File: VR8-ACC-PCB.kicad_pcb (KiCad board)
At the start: 2 copper layers, 140 x 60 mm, 66 parts, among them IC1 LM393P, IC2 VO14642AT, IC3 VO14642AT, IC4 KT12-1A-40L-THT, IC5 NE555P, J1 43650-0516, J2 43650-0516, J3 43650-0216, J4 43650-0416, J5 43045-1013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

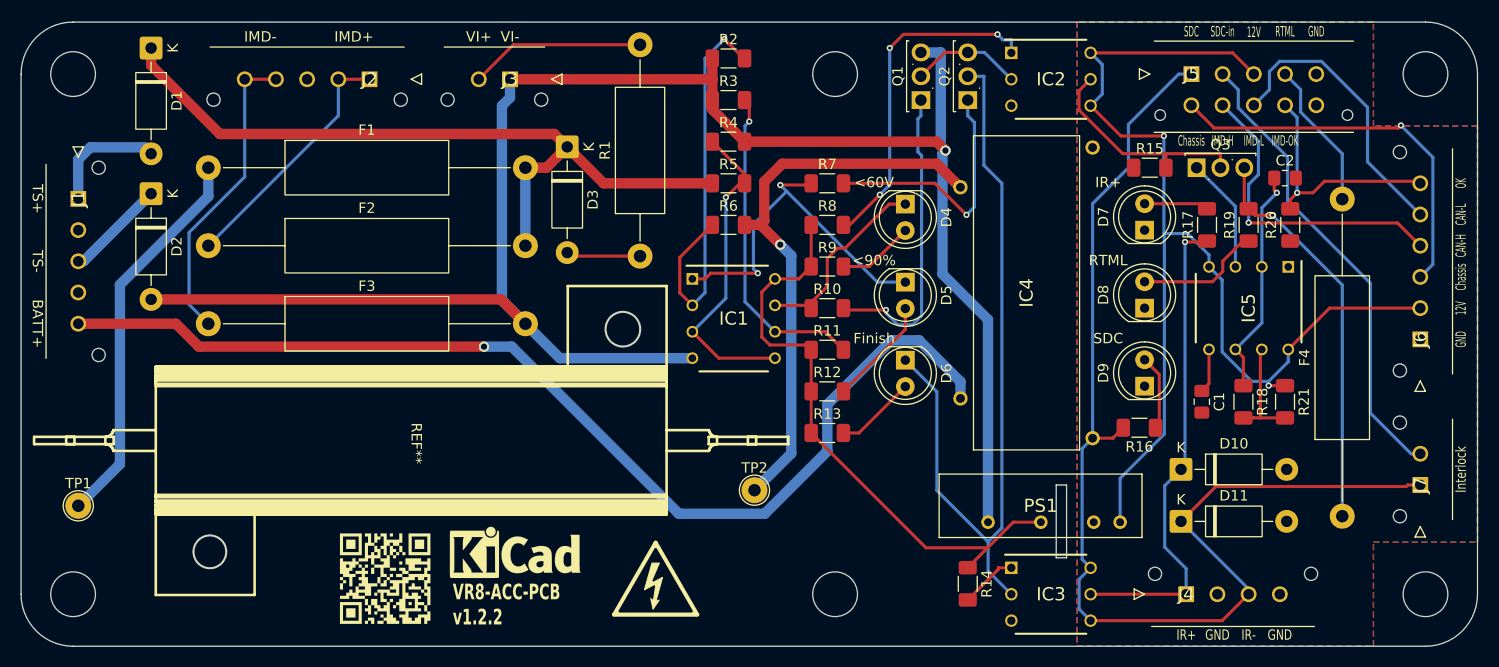
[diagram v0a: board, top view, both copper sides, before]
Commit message: J5 reorientation
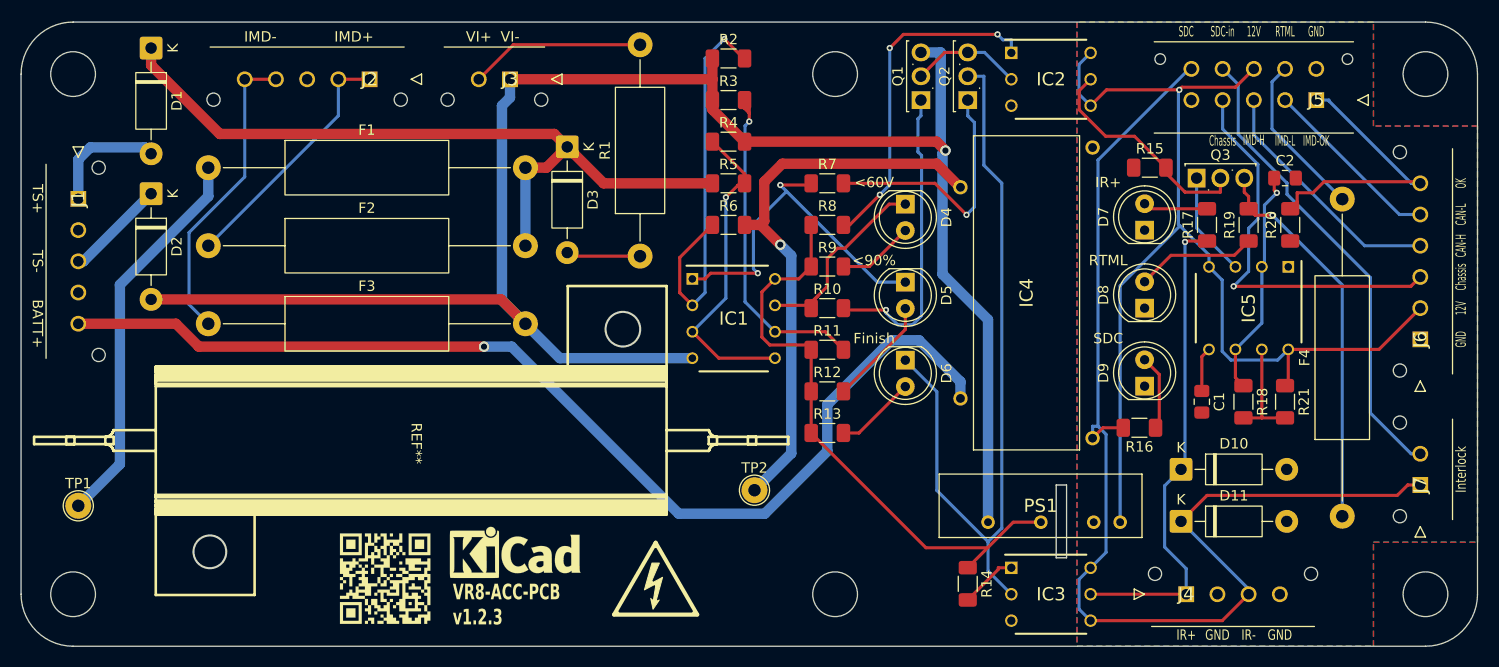
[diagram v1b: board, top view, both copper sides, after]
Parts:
- moved J5 12.3 mm to (160.0, 42.5), turned to 0 degrees
- moved Q3 1.00 mm to (148.5, 50.0)
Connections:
- J5 pad 1: SDC_final -> IMD_Status
- J5 pad 10: unconnected-(J5-Pad10) -> SDC_final
- J5 pad 2: SDC_after_MSD -> IMD_CAN_L
- J5 pad 3: GLV_12V -> IMD_CAN_H
- J5 pad 4: RTML -> Chassis_Ground
- J5 pad 5: GND -> unconnected-(J5-Pad5)
- J5 pad 6: Chassis_Ground -> GND
- J5 pad 7: IMD_CAN_H -> RTML
- J5 pad 8: IMD_CAN_L -> GLV_12V
- J5 pad 9: IMD_Status -> SDC_after_MSD
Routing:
- net IMD_CAN_L: track 27.9 -> 17.6 mm
- net IMD_CAN_H: track 30.5 -> 23.8 mm, vias 1 -> 0
- net GLV_12V: track 110.5 -> 105.6 mm, vias 2 -> 1
- net IMD_Status: track 22.8 -> 27.3 mm, vias 1 -> 0
- net RTML: track 14.3 -> 15.8 mm
- net Net-(IC1-2IN-): track 30.5 -> 31.9 mm
- net SDC_final: track 112.1 -> 113.4 mm
- net Chassis_Ground: track 37.5 -> 38.6 mm
- net Net-(IC5-OUT): track 11.1 -> 10.1 mm
- net OK_60V: track 18.1 -> 19.0 mm
- net SDC_after_MSD: track 44.9 -> 45.4 mm
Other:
- board text added: "VR8-ACC-PCB v1.2.3"
- board text removed: "VR8-ACC-PCB v1.2.2"

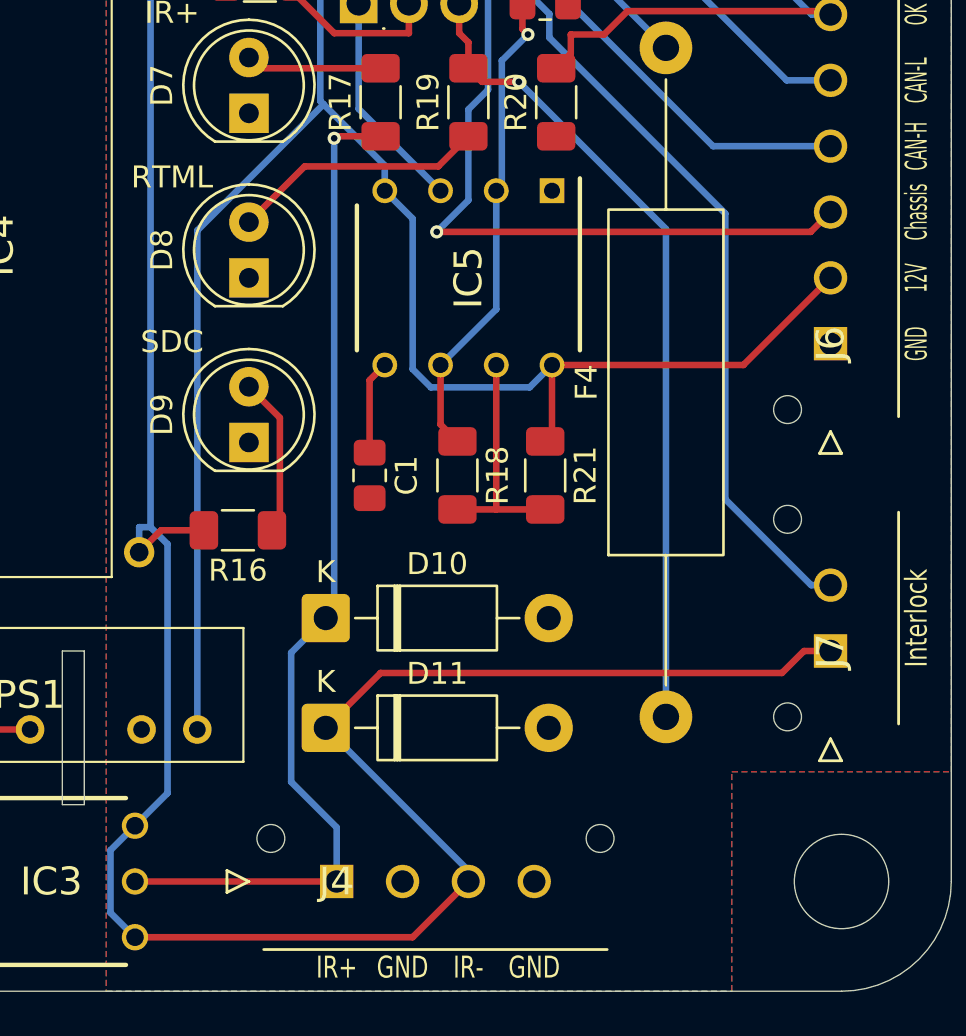
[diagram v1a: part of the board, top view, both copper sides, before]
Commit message: J4 reorientation
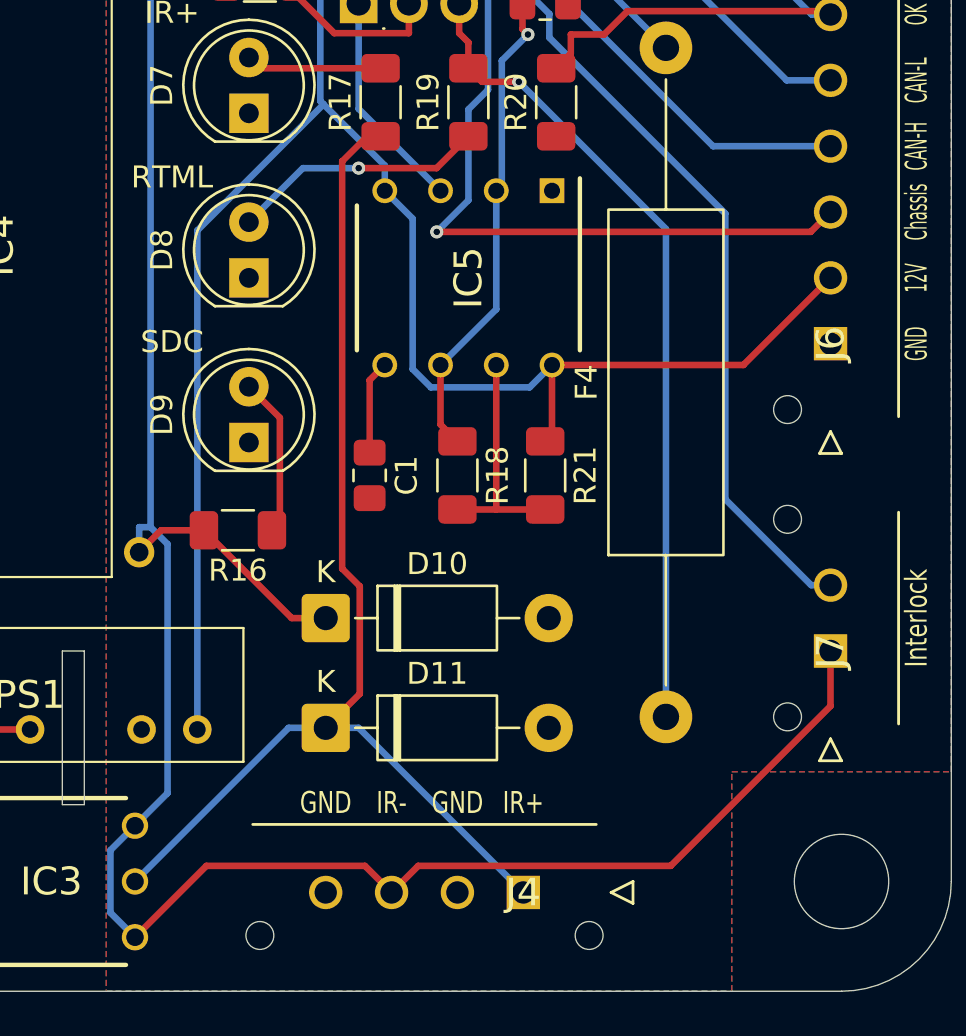
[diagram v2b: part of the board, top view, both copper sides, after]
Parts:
- moved J4 8.51 mm to (156.0, 90.5), turned to 0 degrees
- moved D10 5.00 mm to (147.0, 78.0)
- moved D11 5.00 mm to (147.0, 83.0)
- renumbered D11 to D10, D10 to D11
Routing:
- net IR+_ctrl: track 46.3 -> 52.1 mm, vias 1 -> 0
- net SDC_final: track 113.4 -> 110.3 mm
- net Net-(D8-A): vias 0 -> 1

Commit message: update version
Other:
- board text added: "VR8-ACC-PCB v1.2.4"
- board text removed: "VR8-ACC-PCB v1.2.3"
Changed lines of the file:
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@@
 		)
 	)
-	(gr_text "VR8-ACC-PCB\nv1.2.3"
+	(gr_text "VR8-ACC-PCB\nv1.2.4"
 		(at 77 91 0)
 		(layer "F.SilkS")

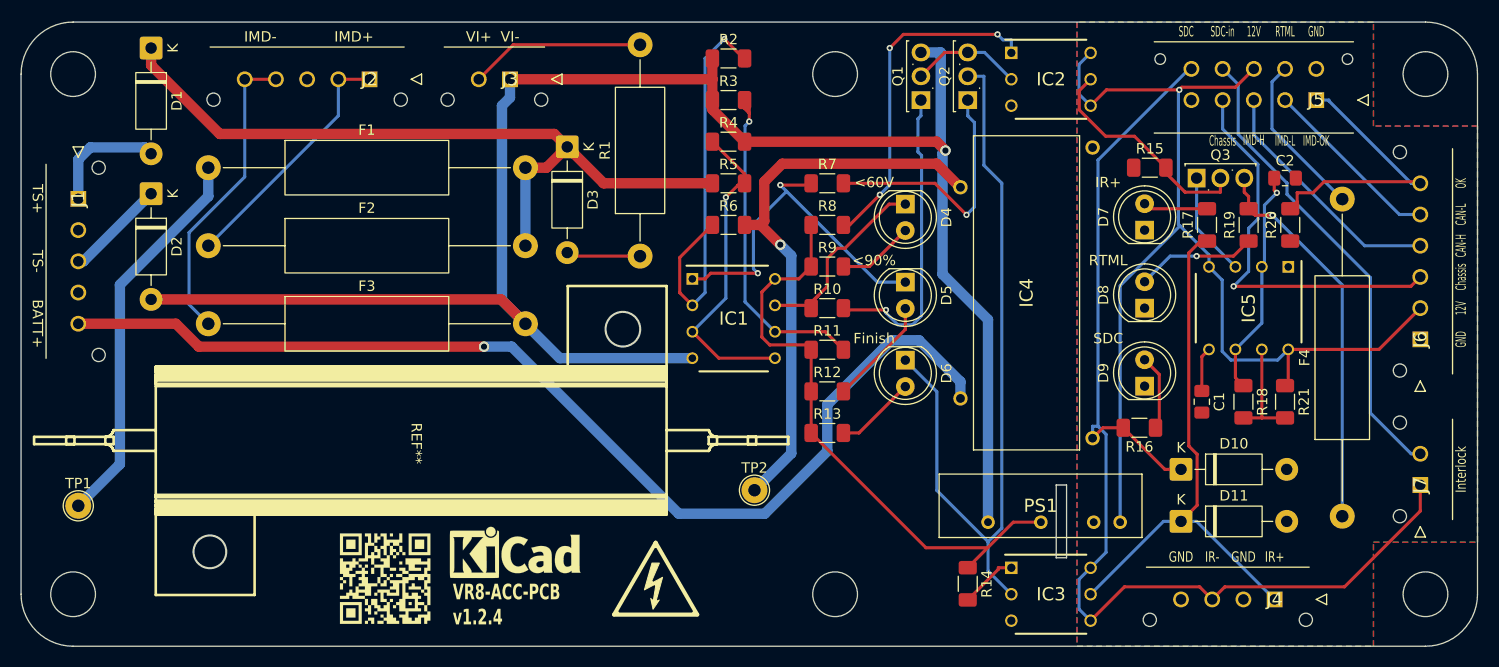
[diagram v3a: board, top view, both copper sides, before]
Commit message: add ne555 output resister
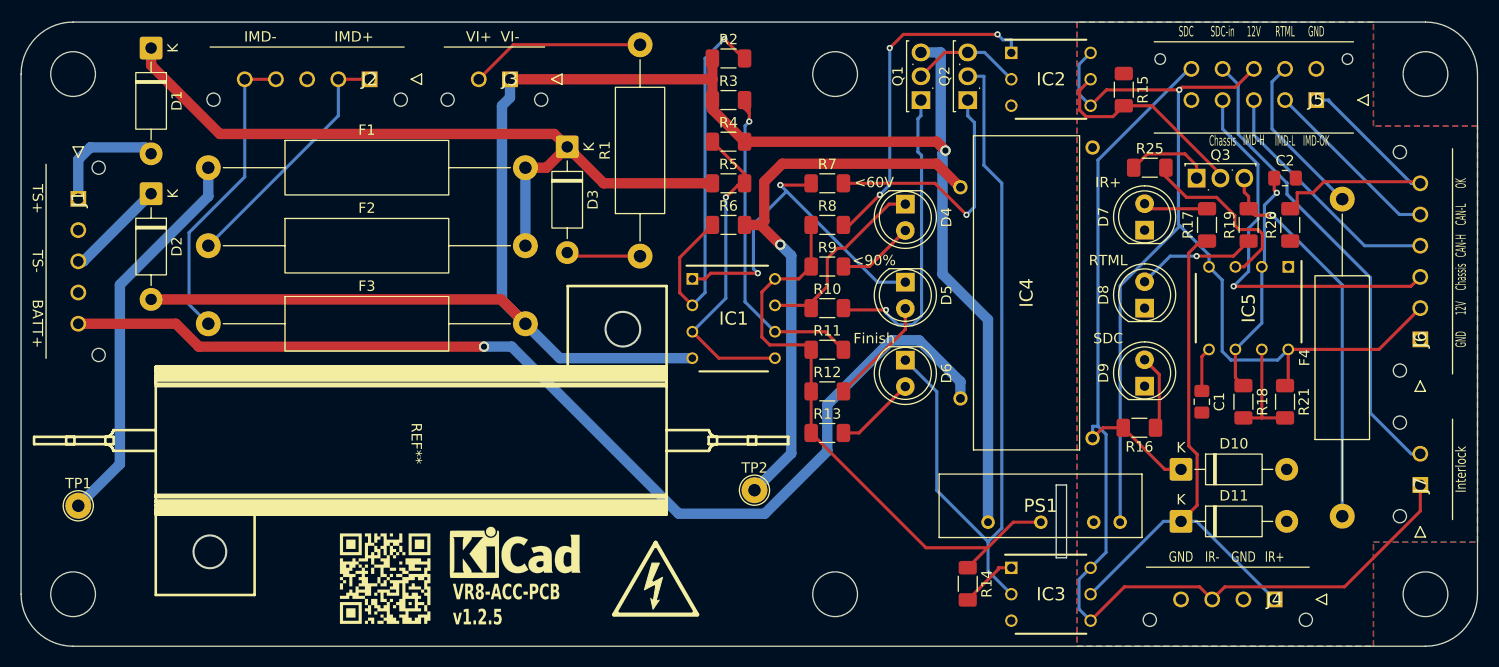
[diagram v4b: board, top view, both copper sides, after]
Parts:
- added R25: 10k, Resistor_SMD:R_1206_3216Metric_Pad1.30x1.75mm_HandSolder, F.Cu at (144.0, 49.0)
- moved R15 7.91 mm to (141.5, 41.5), turned to -90 degrees
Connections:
- Q3 pad 1: Net-(IC5-OUT) -> Net-(Q3-G)
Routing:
- net Net-(Q3-G): track 0.00 -> 8.27 mm
- net Net-(IC5-OUT): track 10.1 -> 17.7 mm
- net RTML_enable: track 21.4 -> 20.7 mm
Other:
- board text added: "GLV"
- board text added: "VR8-ACC-PCB v1.2.5"
- board text removed: "LV"
- board text removed: "VR8-ACC-PCB v1.2.4"

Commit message: fix wrong DCDC & precharge relay pin connection
swap out +/out - of the DCDC
swap coil/contact of the relay
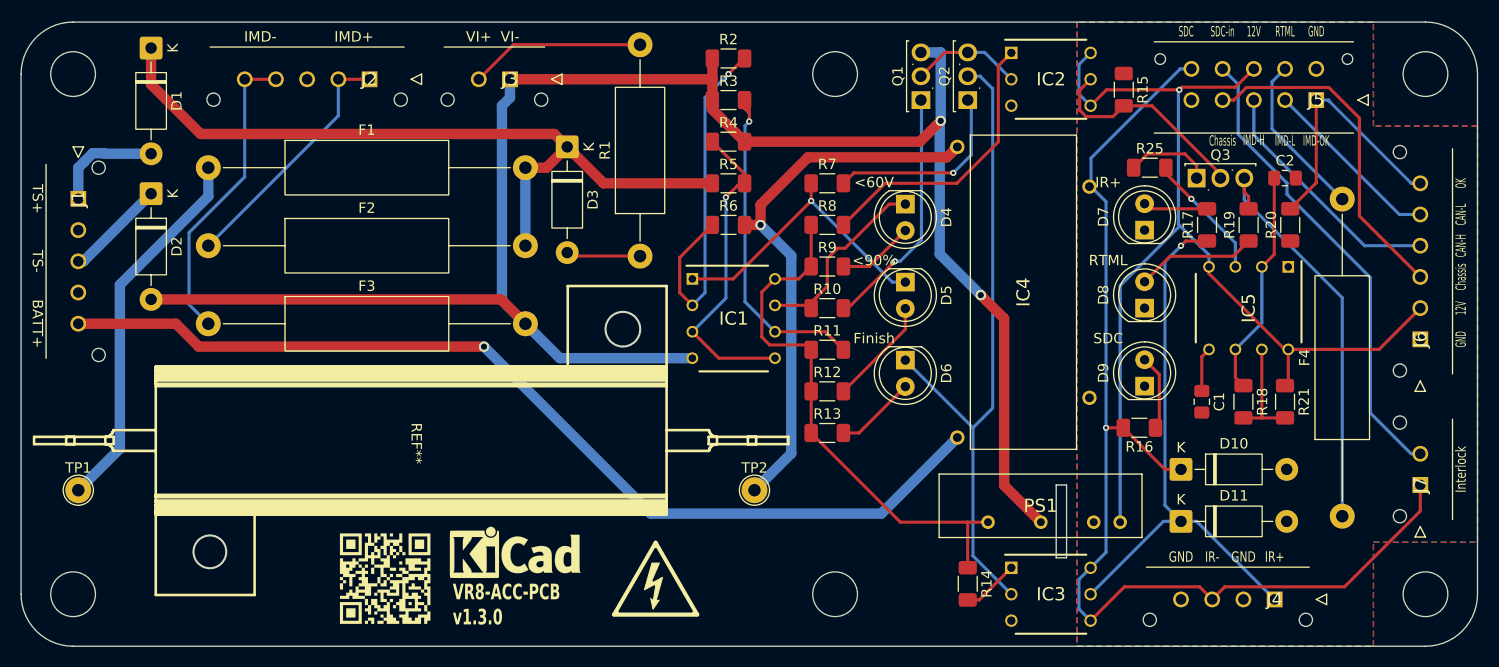
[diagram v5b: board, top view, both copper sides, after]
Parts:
- moved IC4 30.9 mm to (125.5, 47.0), turned to -90 degrees
- moved TP1 1.50 mm to (41.0, 80.0)
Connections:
- IC4 pad 1: SDC_final -> HV+
- IC4 pad 2: GND -> BATT+
- IC4 pad 3: HV+ -> GND
- IC4 pad 4: BATT+ -> SDC_final
- PS1 pad 4: HV_12V -> TS-
- PS1 pad 6: TS- -> HV_12V
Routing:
- net Net-(D6-K): track 74.3 -> 63.0 mm
- net BATT+: track 105.2 -> 95.1 mm
- net Net-(Q2-G): track 24.7 -> 18.3 mm
- net OK_90%: track 34.6 -> 28.3 mm, vias 2 -> 1
- net Chassis_Ground: track 38.6 -> 32.6 mm, vias 1 -> 0
- net Net-(Q1-G): track 29.4 -> 23.4 mm
- net Net-(IC5-OUT): track 17.7 -> 11.7 mm, vias 0 -> 1
- net Net-(IC2-A): track 32.9 -> 27.3 mm, vias 3 -> 0
- net HV_12V: track 57.1 -> 51.6 mm
- net GLV_12V: track 105.6 -> 100.8 mm
- net Net-(IC1-1IN-): track 39.0 -> 35.3 mm
- net IMD_Status: track 27.3 -> 24.8 mm
- net Net-(Q3-S): track 37.4 -> 39.5 mm, vias 1 -> 0
- net SDC_final: track 110.3 -> 108.2 mm, vias 0 -> 1
- net IR+_ctrl: track 52.1 -> 54.2 mm, vias 0 -> 1
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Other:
- board text added: "VR8-ACC-PCB v1.3.0"
- board text removed: "VR8-ACC-PCB v1.2.5"

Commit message: find and fix test errors, some improvement
1. remove onboard fuse (now is inline)
2. change RTML nmos to pmos (to make nmos on, RTML only have V_G-V_th=10V, which is not enough to drive RTML)
3. new voltage divider config (resistors tolerance is matter, <1% is better)
4. add IR+_ctrl signal output to J5
5. J7 is now used for powering Arduino rather than bridging interlock signal (SDC_after_MSD is removed from J5 as well)
6. explain the working principle on sch
7. move to kicad 10
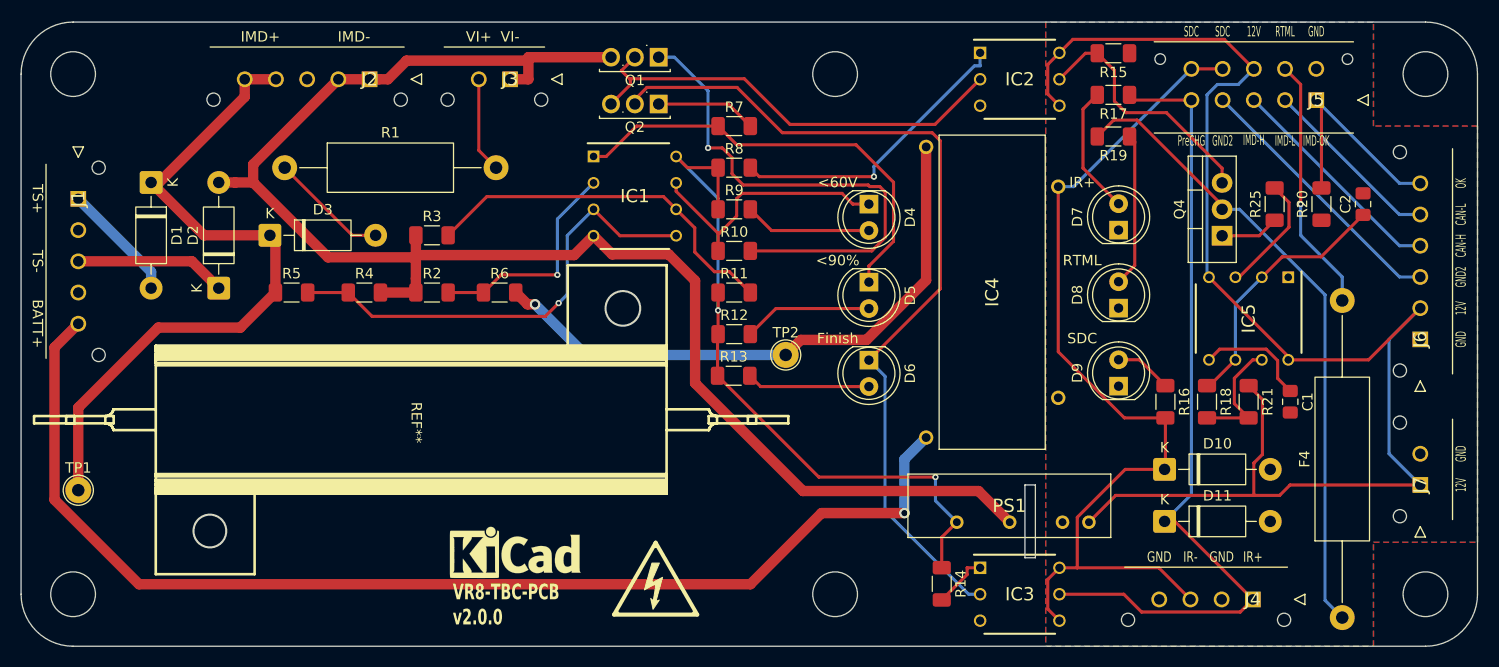
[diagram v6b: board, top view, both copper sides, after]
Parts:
- removed F1, F2, F3: Fuse, Resistor_THT:R_Axial_DIN0516_L15.5mm_D5.0mm_P30.48mm_Horizontal
- removed Q3: Q_NMOS_Depletion_GDS, Package_TO_SOT_THT:TO-251-3_Vertical
- removed QR*****: github, custom:github
- added Q4: Q_PMOS_GDS, Package_TO_SOT_THT:TO-220-3_Vertical, F.Cu at (150.9, 55.5)
- R1: value 360k -> 200k
- moved R5 43.3 mm to (61.5, 61.0)
- moved R4 37.9 mm to (68.5, 61.0)
- moved R2 36.3 mm to (75.0, 61.0)
- moved R1 35.2 mm to (60.8, 49.0), turned to 0 degrees
- moved R3 31.3 mm to (75.0, 55.5)
- moved D3 29.8 mm to (59.4, 55.5), turned to 0 degrees
- moved Q2 29.7 mm to (96.8, 42.9), turned to 180 degrees
- moved Q1 25.5 mm to (96.8, 38.4), turned to 180 degrees
- moved R6 22.9 mm to (81.5, 61.0)
- moved R19 15.5 mm to (140.5, 46.0), turned to 180 degrees
- moved R17 15.4 mm to (140.5, 42.0), turned to 180 degrees
- moved IC1 15.1 mm to (94.5, 51.7)
- moved TP2 13.3 mm to (109.0, 67.0)
- moved D1 12.9 mm to (48.0, 50.4)
- moved R25 12.5 mm to (156.0, 52.5), turned to 90 degrees
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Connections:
- J2 pad 1: Net-(F2-Pad1) -> TS-
- J2 pad 2: Net-(F2-Pad1) -> TS-
- J2 pad 4: Net-(F3-Pad1) -> TS+
- J2 pad 5: Net-(F3-Pad1) -> TS+
- J5 pad 5: unconnected-(J5-Pad5) -> IR+_ctrl
- J5 pad 9: SDC_after_MSD -> SDC_final
- J7 pad 1: SDC_final -> GLV_12V
- J7 pad 2: SDC_after_MSD -> GND
- TP1 pad 1: Net-(F1-Pad1) -> TS+
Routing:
- net SDC_after_MSD: track 45.4 -> 0.00 mm
- net GLV_12V: track 100.8 -> 139.1 mm, vias 1 -> 0
- net Net-(F1-Pad1): track 36.2 -> 0.00 mm
- net Net-(IC2-K): track 10.7 -> 43.4 mm
- net Net-(F3-Pad1): track 29.5 -> 0.00 mm
- net TS-: track 178.7 -> 150.0 mm, vias 2 -> 0
- net Net-(Q1-G): track 23.4 -> 49.1 mm
- net IR+_ctrl: track 54.2 -> 78.4 mm, vias 1 -> 0
- net Net-(F2-Pad1): track 24.2 -> 0.00 mm
- net Net-(Q4-D): track 39.5 -> 61.1 mm
- net Net-(D6-K): track 63.0 -> 83.5 mm
- net SDC_final: track 108.2 -> 89.2 mm, vias 1 -> 0
- net BATT+: track 95.1 -> 113.9 mm
- net HV_12V: track 51.6 -> 68.0 mm, vias 0 -> 2
- net Net-(IC1-1IN+): track 30.4 -> 45.0 mm
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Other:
- outline, holes or cut-outs redrawn
- board text added: "GND2"
- board text added: "PreCHG"
- board text added: "TS"
- board text added: "VR8-TBC-PCB v2.0.0"
- board text removed: "Chassis"
- board text removed: "HV"
- board text removed: "Interlock"
- board text removed: "SDC-in"
- board text removed: "VR8-ACC-PCB v1.3.0"
